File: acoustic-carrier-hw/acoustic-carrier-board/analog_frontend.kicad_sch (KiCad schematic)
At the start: 47 parts, among them J1 8P8C_Shielded, U2 THS4521IDGK, U3 DGQ2788AEN-T1-GE4, U5 LMV321

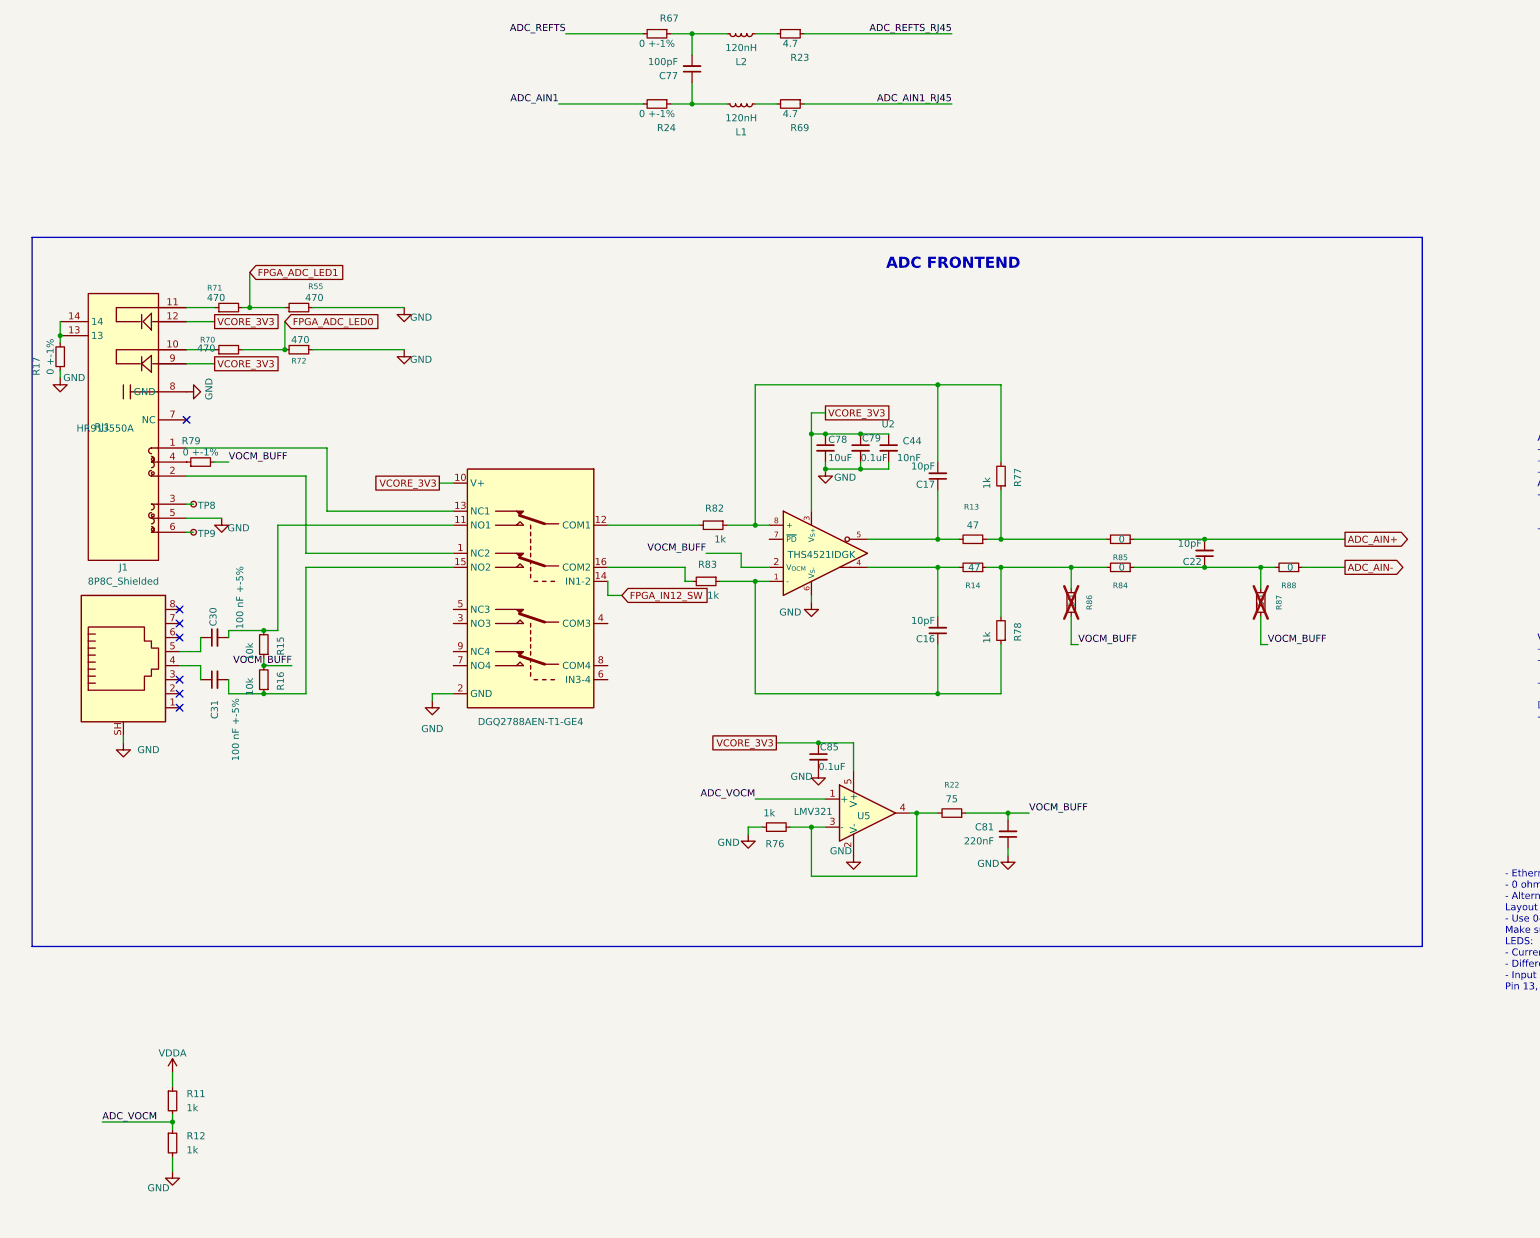
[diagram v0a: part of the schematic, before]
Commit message: [carrier] Replaced voltage reference, added extra 0 ohm resistors, added test-connectors for ADC testing
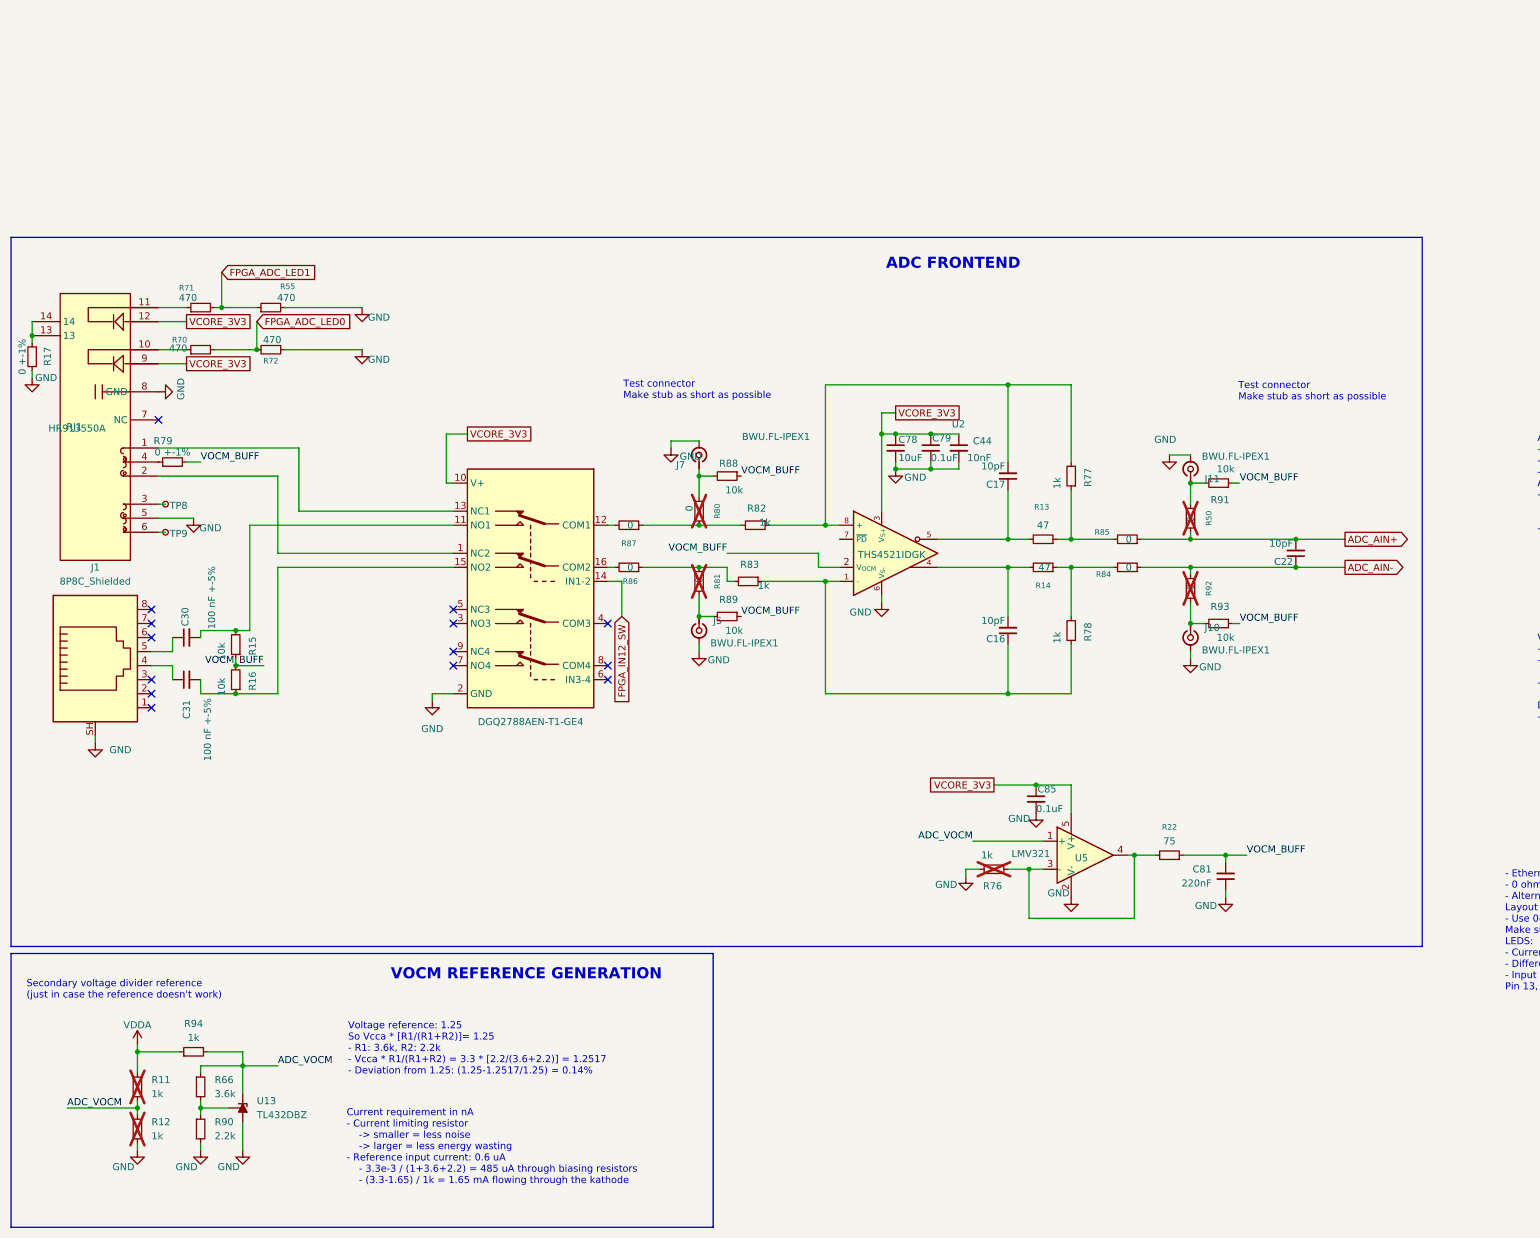
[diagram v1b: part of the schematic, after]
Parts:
- removed C77: 100pF, Capacitor_SMD:C_0603_1608Metric_Pad1.08x0.95mm_HandSolder, symbol Device:C_Small
- removed L1, L2: 120nH, Inductor_SMD:L_0603_1608Metric_Pad1.05x0.95mm_HandSolder, symbol Device:L_Small
- removed R23, R69: 4.7, Resistor_SMD:R_0603_1608Metric_Pad0.98x0.95mm_HandSolder, symbol Device:R_Small
- removed R24, R67: 0 +-1%, Resistor_SMD:R_0805_2012Metric_Pad1.20x1.40mm_HandSolder, symbol Device:R_Small
- added J10, J11, J5, J7: BWU.FL-IPEX1, fpga:BWU.FL-IPEX1, symbol Connector:Conn_Coaxial_Small
- added R50, R80, R81, R92: 0, Resistor_SMD:R_0603_1608Metric, symbol Device:R_Small
- added R66: 3.6k, Resistor_SMD:R_0603_1608Metric, symbol Device:R_Small
- added R89, R91, R93: 10k, Resistor_SMD:R_0603_1608Metric, symbol Device:R_Small
- added R90: 2.2k, Resistor_SMD:R_0603_1608Metric, symbol Device:R_Small
- added R94: 1k, Resistor_SMD:R_0603_1608Metric, symbol Device:R_Small
- added U13: TL432DBZ, Package_TO_SOT_SMD:SOT-23, symbol Reference_Voltage:TL432DBZ
- R11, R12, R76: now not fitted; now left out of the parts list
- R86, R87: value 50 -> 0; LPN (none) -> C21189; MPN (none) -> 0603WAF0000T5E; now fitted; now in the parts list
- R88: value 0 -> 10k; LPN C21189 -> C25804; MPN 0603WAF0000T5E -> 0603WAF1002T5E
- U3: footprint (none) -> fpga:QFN40P260X180X60-16N_Fv1.2; LPN (none) -> C2673179; MPN (none) -> DGQ2788AEN-T1-GE4
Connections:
- net ADC_AIN+: now also R50.1
- net ADC_AIN-: now also C22.1, R84.1, R92.1; no longer R88.1
- net ADC_VOCM: now also R66.1, R94.2, U13.2 (K)
- net GND: now also J10.2 (Ext), J11.2 (Ext), J5.2 (Ext), J7.2 (Ext), R90.2, U13.3 (A)
- net VDDA: now also R94.1
- net VOCM_BUFF: now also R88.1, R89.1, R91.1, R93.1; no longer R86.2, R87.2
- net at R14.1, R78.2, R84.2: no longer R86.1
- net at R82.2: now also R87.1, R80.2; no longer U3.12 (COM1)
- net at R83.2: now also R86.1, R81.1; no longer U3.16 (COM2)
- new net: J5.1 (In), R81.2, R89.2
- new net: R66.2, R90.1, U13.1 (REF)
- new net: J11.1 (In), R50.2, R91.2
- new net: J7.1 (In), R80.1, R88.2
- new net: R87.2, U3.12 (COM1)
- new net: R86.2, U3.16 (COM2)
- new net: J10.1 (In), R92.2, R93.2
- no-connect marks 7 -> 14
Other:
- note added: "Current requirement in nA - Current limiting resistor -> smaller = less noise -> larger = less energy wasting - Reference input current: 0.6 uA - 3.3e-3 / (1+3.6+2.2) = 485 uA through biasing resistors - (3.3-1.65) / 1k = 1.65 mA flowing through the kathode"
- note added: "Secondary voltage divider reference (just in case the reference doesn't work)"
- note added: "Test connector Make stub as short as possible"
- note added: "VOCM REFERENCE GENERATION"
- note added: "Voltage reference: 1.25 So Vcca * [R1/(R1+R2)]= 1.25 - R1: 3.6k, R2: 2.2k - Vcca * R1/(R1+R2) = 3.3 * [2.2/(3.6+2.2)] = 1.2517 - Deviation from 1.25: (1.25-1.2517/1.25) = 0.14%"
- moved on the sheet: C16, C17, C22, C30, C31, C44, C78, C79, C81, C85, J1, R13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

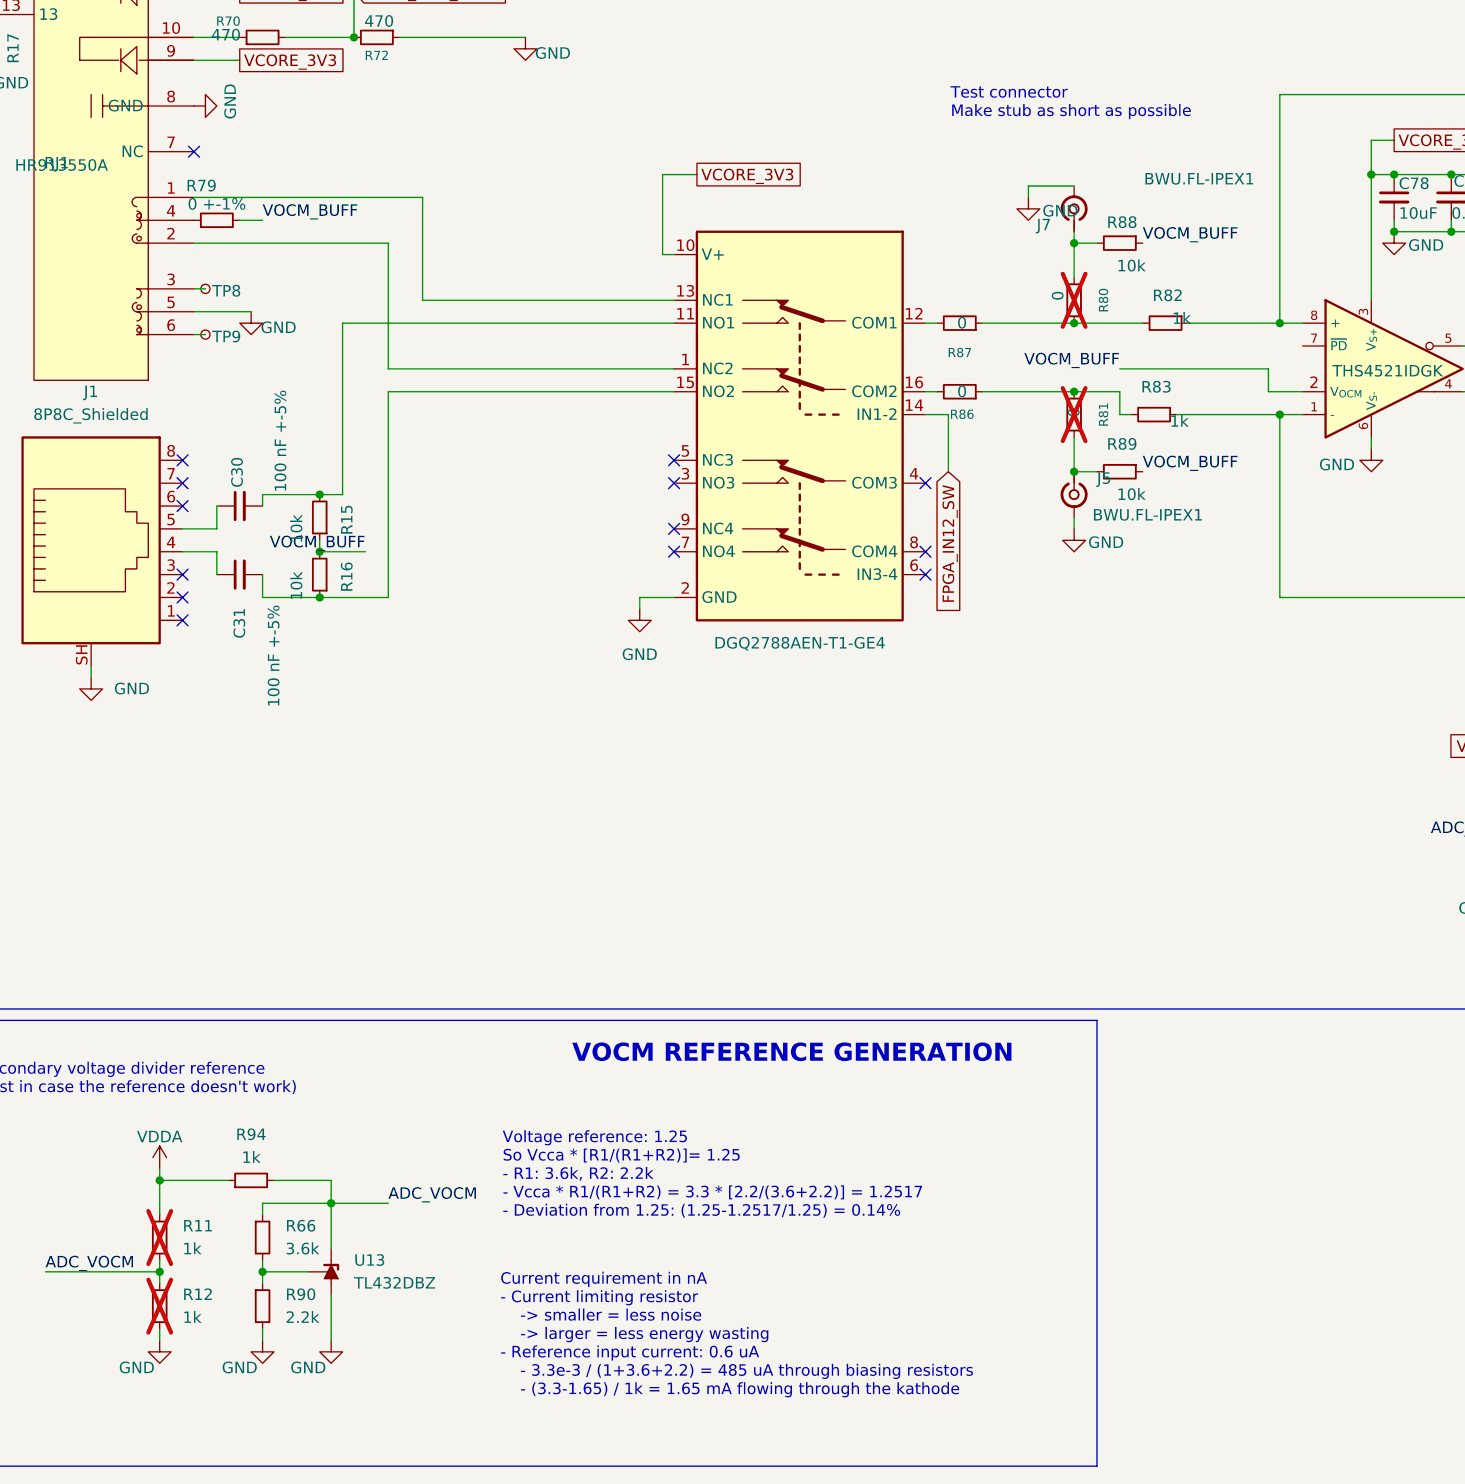
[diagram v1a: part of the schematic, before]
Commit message: [carrier] Fixed ERC issues, added PDn pin connection
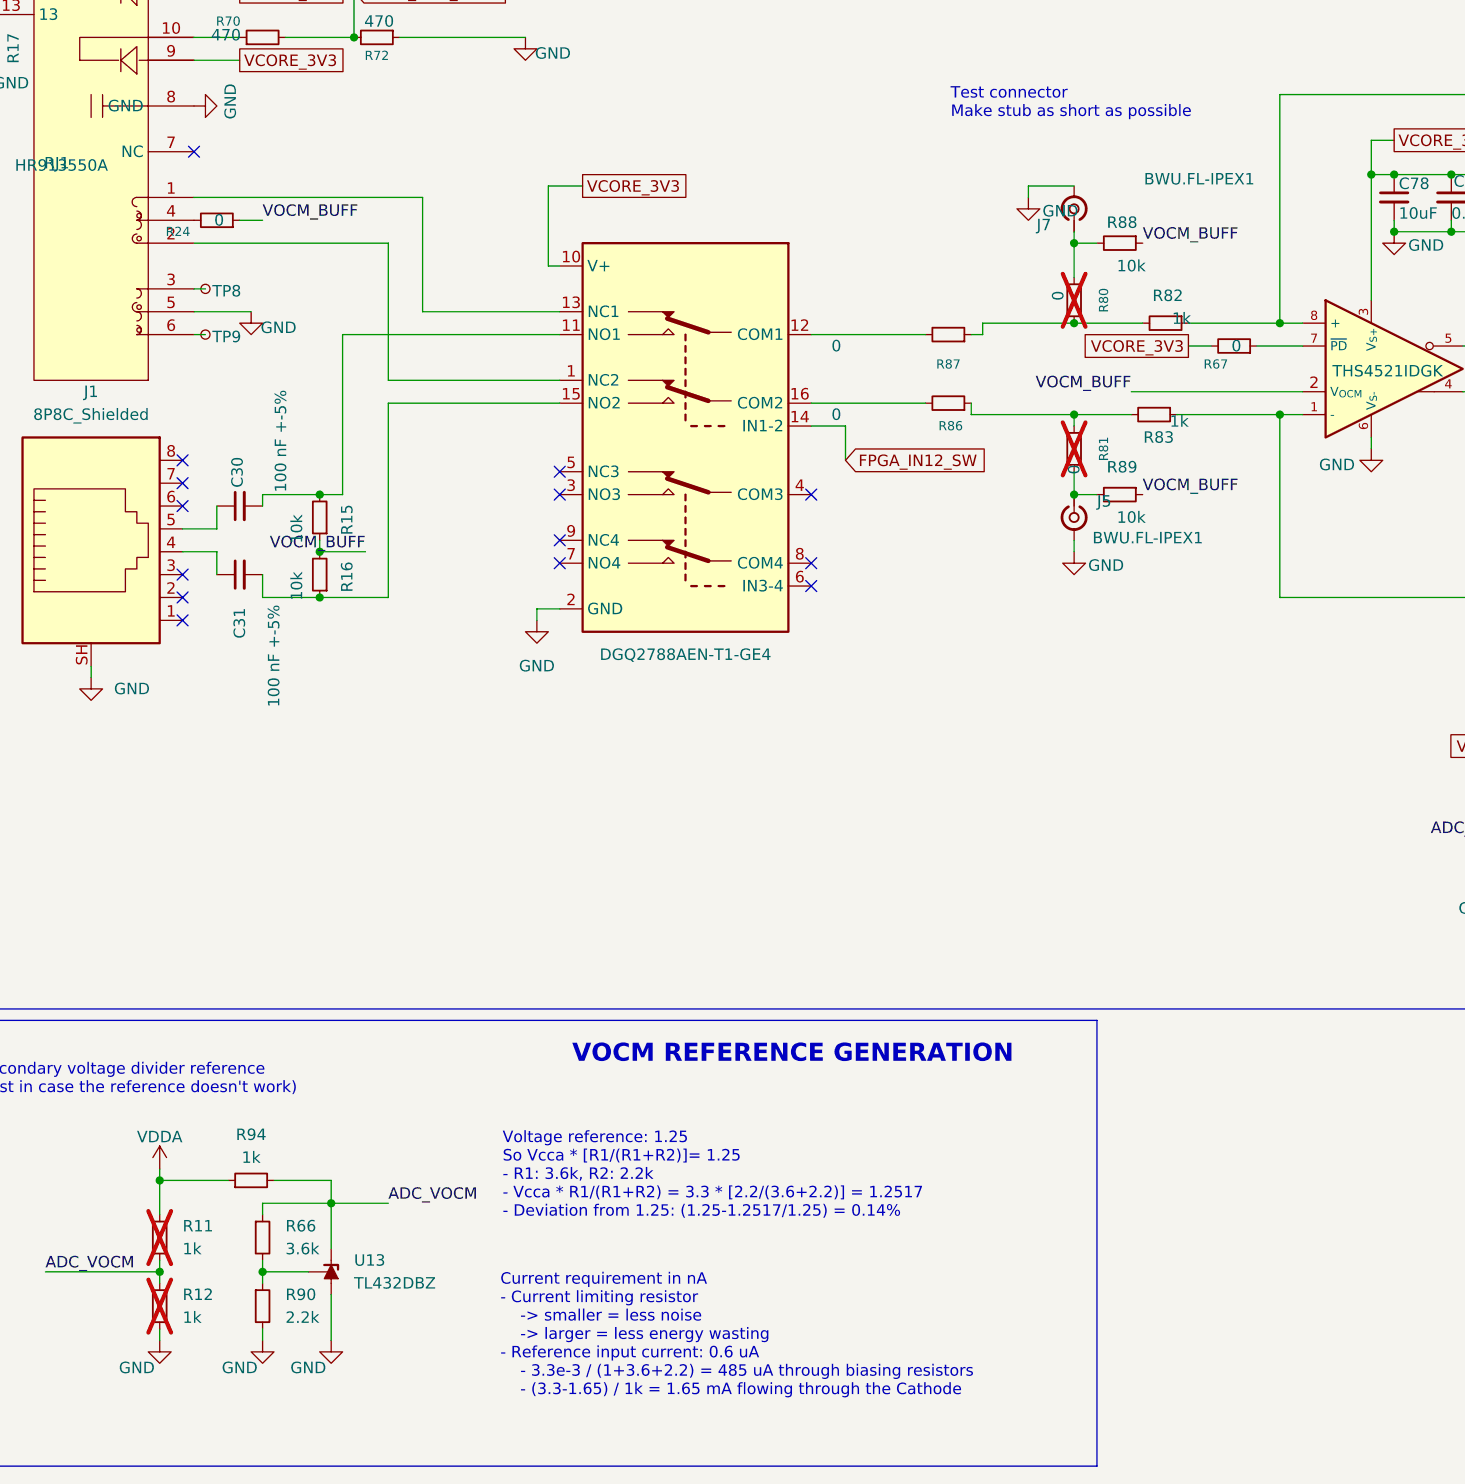
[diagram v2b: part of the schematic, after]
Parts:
- removed R79: 0 +-1%, Resistor_SMD:R_0805_2012Metric_Pad1.20x1.40mm_HandSolder, symbol Device:R_Small
- added R24, R67: 0, Resistor_SMD:R_0603_1608Metric, symbol Device:R_Small
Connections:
- net VCORE_3V3: now also R67.2
- net VOCM_BUFF: now also R24.1
- net at U2.7 (~{PD}): now also R67.1
- net at RJ1.4: now also R24.2
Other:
- note added: "Current requirement in nA - Current limiting resistor -> smaller = less noise -> larger = less energy wasting - Reference input current: 0.6 uA - 3.3e-3 / (1+3.6+2.2) = 485 uA through biasing resistors - (3.3-1.65) / 1k = 1.65 mA flowing through the Cathode"
- note removed: "Current requirement in nA - Current limiting resistor -> smaller = less noise -> larger = less energy wasting - Reference input current: 0.6 uA - 3.3e-3 / (1+3.6+2.2) = 485 uA through biasing resistors - (3.3-1.65) / 1k = 1.65 mA flowing through the kathode"
- moved on the sheet: J5, R81, R86, R87, R89
